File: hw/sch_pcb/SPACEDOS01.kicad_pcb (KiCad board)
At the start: 2 copper layers, 93.5 x 48.2 mm, 92 parts, among them J1 HEADER_2x01, J19 HEADER_2x01_PARALLEL, J2 HEADER_2x01_PARALLEL, J22 HEADER_2x03, J3 HEADER_2x01_PARALLEL, J4 HEADER_1x01, J5 HEADER_1x01, J6 HEADER_1x01, J7 HEADER_1x01, M1 HOLE, M10 BMI-S-204-F, M2 HOLE, M3 HOLE, M4 HOLE, M6 BMI-S-210-F, M8 BMI-S-204-F, M9 BMI-S-204-F, U1 OPA2314, U10 ATMEGA1284P-AU, U11 PCF85263A, U2 OPA2314, U3 ISL21080DIH312Z-TK 1V25, U4 TS7211, U5 TS5A4594, U8 TPS613222ADBV, Y2 ABS07-120-32.768KHZ-T

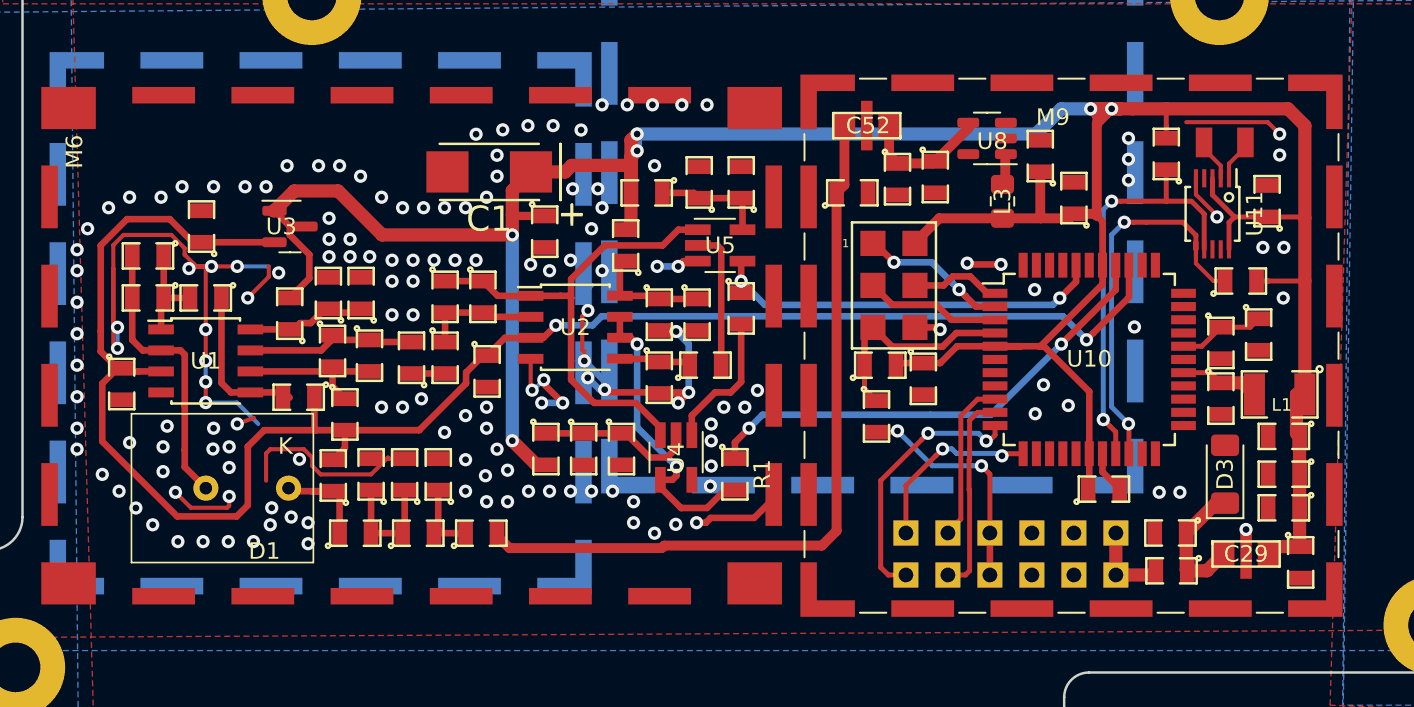
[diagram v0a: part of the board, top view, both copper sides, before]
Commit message: Update project. Update components IDs
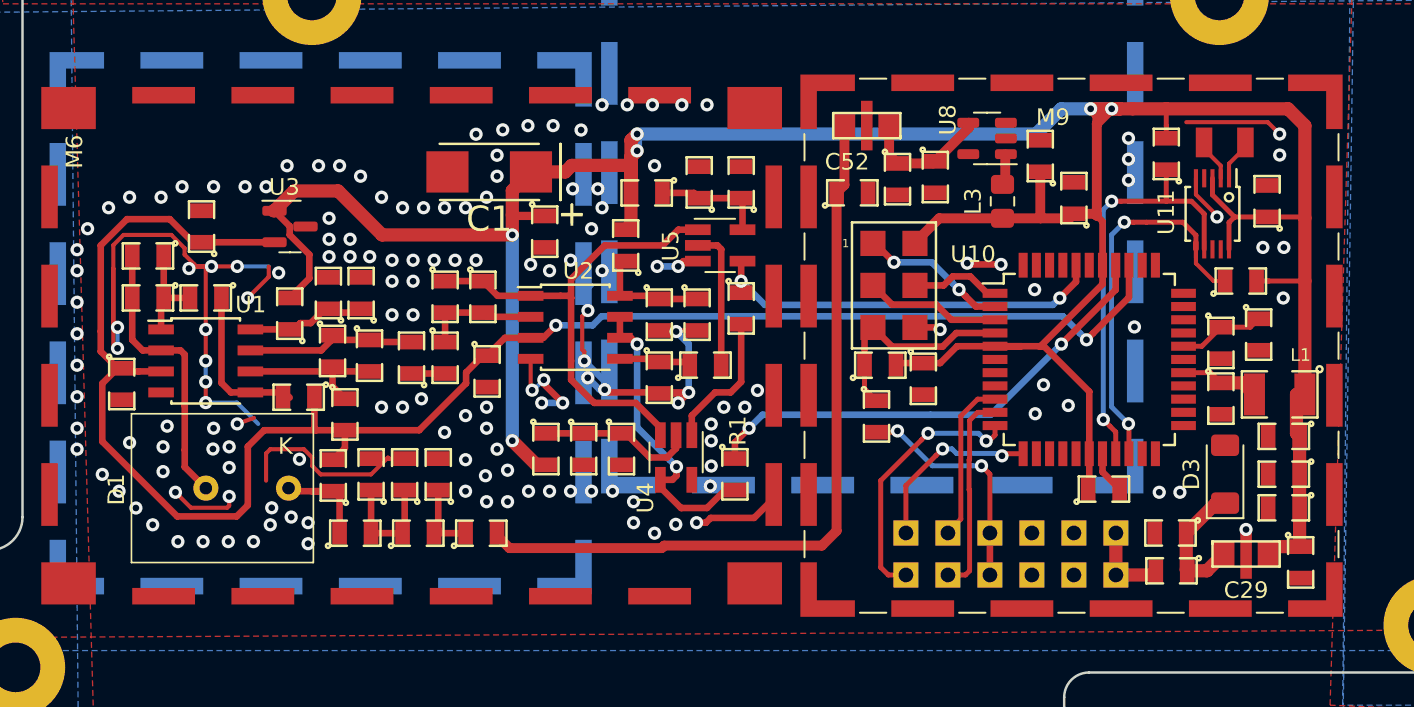
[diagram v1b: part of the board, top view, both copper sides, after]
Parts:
- D1: value S11773-02 -> S2744-09
- R10: value 1k -> 1k2
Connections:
- J1 pad 1: (no net) -> unconnected-(J1-Pad1)
- J1 pad 2: (no net) -> unconnected-(J1-Pad2)
- U10 pad 13: (no net) -> unconnected-(U10-(PCINT28/XCK1/OC1B)PD4-Pad13)
- U10 pad 14: (no net) -> unconnected-(U10-(PCINT294/OC1A)PD5-Pad14)
- U10 pad 15: (no net) -> unconnected-(U10-(PCINT30/OC2B/ICP)PD6-Pad15)
- U10 pad 16: (no net) -> unconnected-(U10-(PCINT31/OC2A)PD7-Pad16)
- U10 pad 21: (no net) -> unconnected-(U10-(PCINT18/TCK)PC2-Pad21)
- U10 pad 22: (no net) -> unconnected-(U10-(PCINT19/TMS)PC3-Pad22)
- U10 pad 23: (no net) -> unconnected-(U10-(PCINT20/TDO)PC4-Pad23)
- U10 pad 24: (no net) -> unconnected-(U10-(PCINT21/TDI)PC5-Pad24)
- U10 pad 25: (no net) -> unconnected-(U10-(PCINT22/TOSC1)PC6-Pad25)
- U10 pad 26: (no net) -> unconnected-(U10-(PCINT23/TOSC2)PC7-Pad26)
- U10 pad 30: (no net) -> unconnected-(U10-(PCINT7/ADC7)PA7-Pad30)
- U10 pad 31: (no net) -> unconnected-(U10-(PCINT6/ADC6)PA6-Pad31)
- U10 pad 32: (no net) -> unconnected-(U10-(PCINT5/ADC5)PA5-Pad32)
- U10 pad 33: (no net) -> unconnected-(U10-(PCINT4/ADC4)PA4-Pad33)
- U10 pad 34: (no net) -> unconnected-(U10-(PCINT3/ADC3)PA3-Pad34)
- U10 pad 35: (no net) -> unconnected-(U10-(PCINT2/ADC2)PA2-Pad35)
- U10 pad 41: (no net) -> unconnected-(U10-(PCINT9/CLKO/T1)PB1-Pad41)
- U10 pad 42: (no net) -> unconnected-(U10-(PCINT10/AIN0/INT2)PB2-Pad42)
- U10 pad 43: (no net) -> unconnected-(U10-(PCINT11/AIN1/OC0)PB3-Pad43)
- U10 pad 44: (no net) -> unconnected-(U10-(PCINT12/OC0B/~{SS})PB4-Pad44)
- U10 pad 7: (no net) -> unconnected-(U10-XTAL2-Pad7)
- U10 pad 8: (no net) -> unconnected-(U10-XTAL1-Pad8)
- U11 pad 4: (no net) -> unconnected-(U11-TS-Pad4)
- U11 pad 8: (no net) -> unconnected-(U11-CLK-Pad8)
- U11 pad 9: (no net) -> unconnected-(U11-INTA-Pad9)
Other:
- board text added: "2026"
- board text removed: "2019"
- board text removed: "JACHO"
